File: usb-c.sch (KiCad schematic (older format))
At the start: 55 parts, among them J201 USB_C_Receptacle, U201 PTN5110HQZ, U202 PTN36043BXZ, U203 PCMF3HDMI2SZ, U204 PCMF2HDMI2SZ, U205 TLV3201AIDBVR

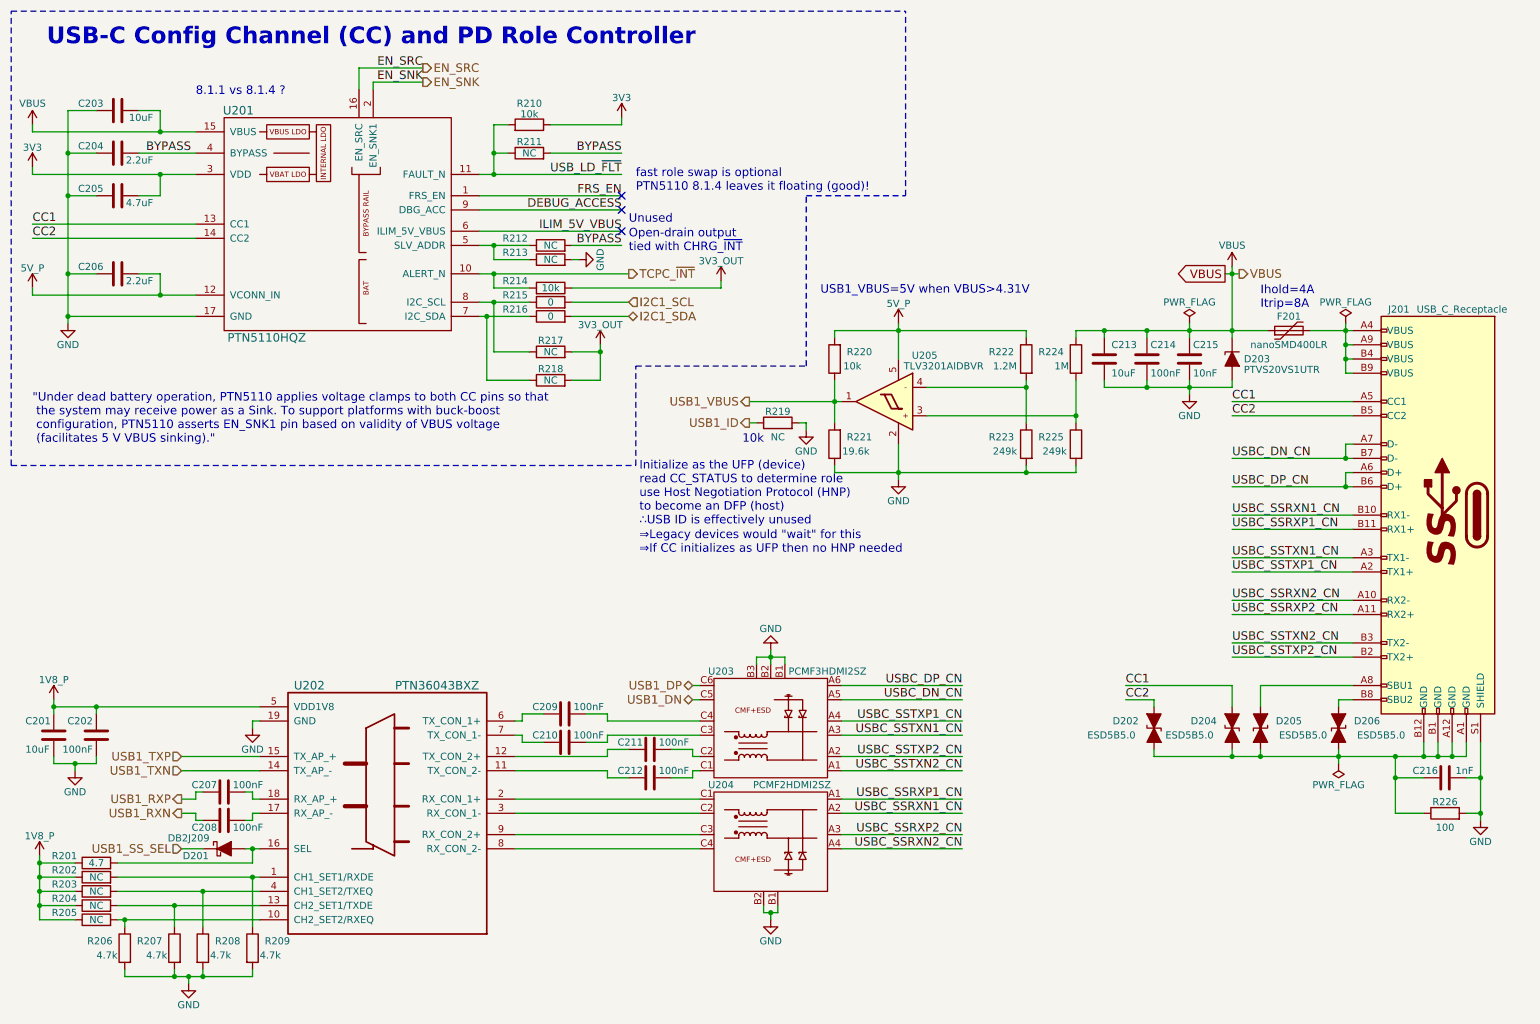
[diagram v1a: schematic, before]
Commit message: Begin GNSS schematic using MAX-M8 module
Since UART2 isn't brought out then will either need to use UART1 (debug) with jumpers or the module's I2C interface.

Resolve merge conflict after pulling recent commit, now can no longer use SSH (since Gogs is getting abandoned?).
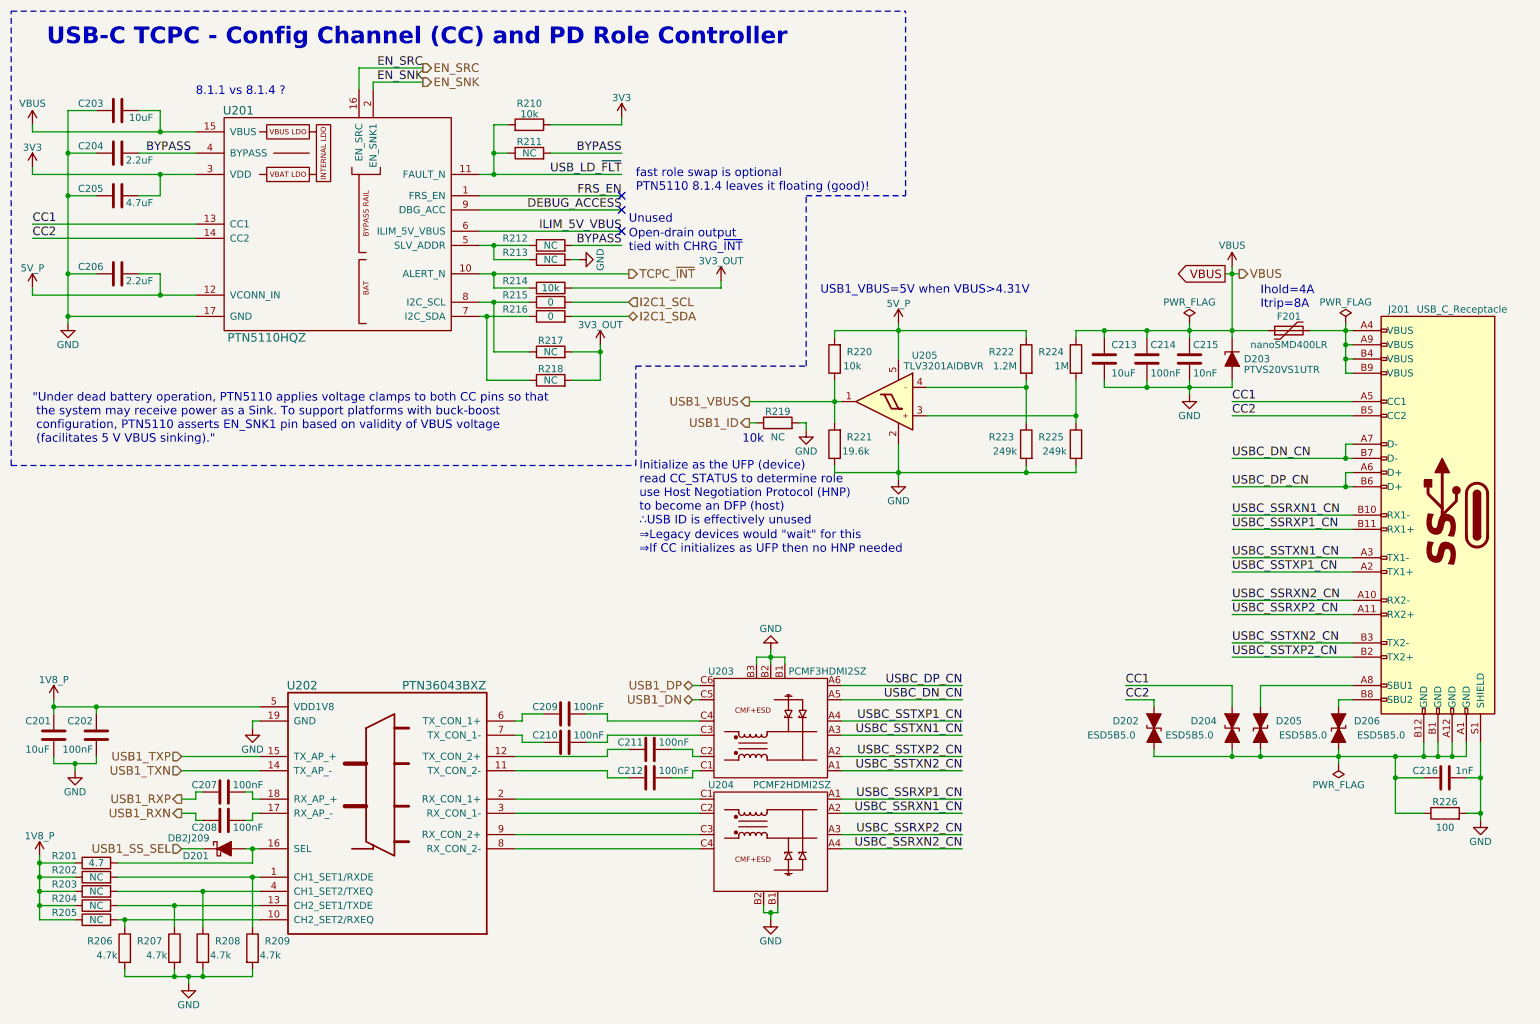
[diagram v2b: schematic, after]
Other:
- note added: "USB-C TCPC - Config Channel (CC) and PD Role Controller"
- note removed: "USB-C Config Channel (CC) and PD Role Controller"
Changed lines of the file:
@@
 $Descr A4 11693 8268
 encoding utf-8
-Sheet 2 23
+Sheet 2 24
 Title "USB Type C"
 Date "2018-05-23"
@@
 Ihold=4A\nItrip=8A
 Text Notes 750  750  0    118  ~ 24
-USB-C Config Channel (CC) and PD Role Controller
+USB-C TCPC - Config Channel (CC) and PD Role Controller
 $Comp
 L USB_C_Receptacle J201
@@
 U 1 1 5AECBE93
 P 3150 6200
-F 0 "U202" H 2600 7150 60  0000 C CNN
-F 1 "PTN36043BXZ" H 3500 7150 60  0000 C CNN
+F 0 "U202" H 2550 7150 60  0000 C CNN
+F 1 "PTN36043BXZ" H 3550 7150 60  0000 C CNN
 F 2 "" H 3150 6350 60  0001 C CNN
 F 3 "https://www.nxp.com/docs/en/data-sheet/PTN36043.pdf" H 3150 6350 60  0001 C CNN

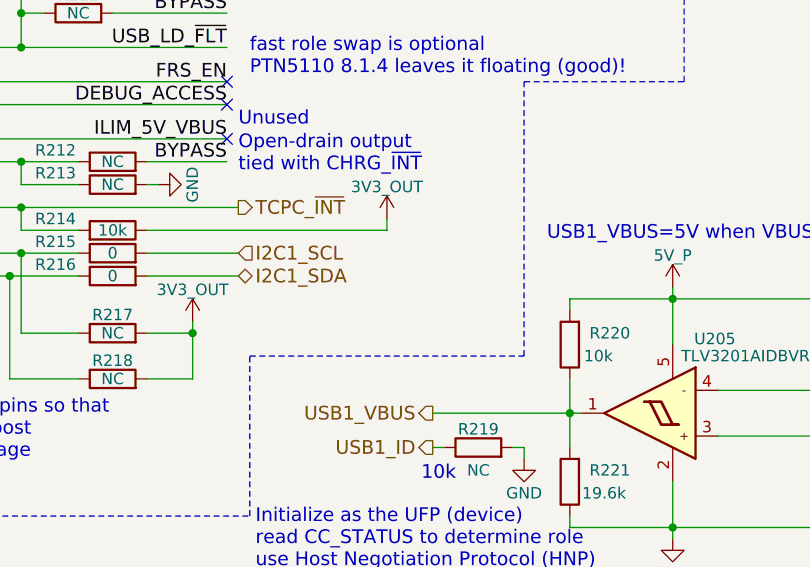
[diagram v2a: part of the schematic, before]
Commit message: Include address in schematic notes for all I2C1 slaves, make HDMI connector shielding resistor to GND 0Ohms
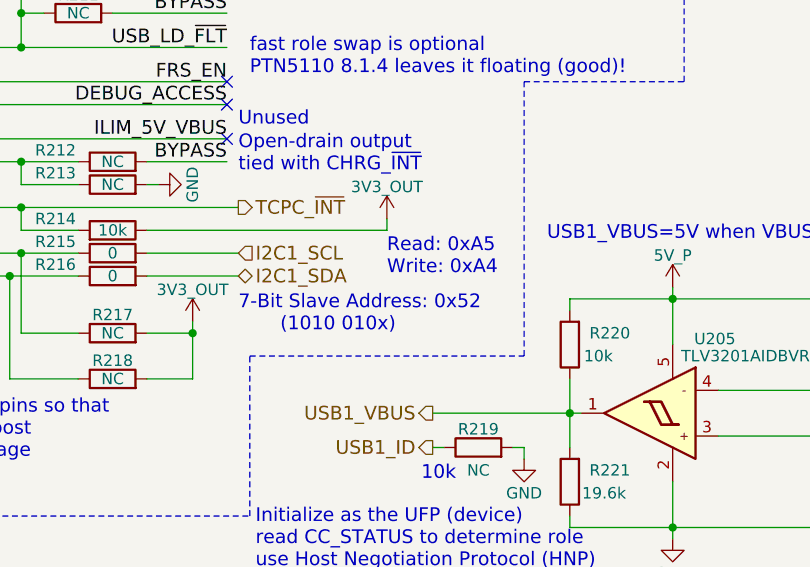
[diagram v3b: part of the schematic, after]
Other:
- note added: "7-Bit Slave Address: 0x52\n (1010 010x)"
- note added: "Read: 0xA5\nWrite: 0xA4"
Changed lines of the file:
@@
 	1    0    0    -1
 $EndComp
+Text Notes 4850 2900 0    60   ~ 0
+7-Bit Slave Address: 0x52\n       (1010 010x)
+Text Notes 5500 2650 0    60   ~ 0
+Read: 0xA5\nWrite: 0xA4
 $EndSCHEMATC

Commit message: Assign most of the capacitors their respective footprints (most are 0603s), add camera/CSI connector component info, source cheaper distributors for 3.5mm headset jack and RJ45
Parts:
- C202, C204, C205, C206, C207, C208, C209, C210, C211, C212, C214, C215, C216: footprint (none) -> Capacitors_SMD:C_0603
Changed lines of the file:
@@
 F 0 "C204" V 1300 1600 50  0000 L CNN
 F 1 "2.2uF" V 1200 1250 50  0000 L CNN
-F 2 "" H 1288 1350 50  0001 C CNN
+F 2 "Capacitors_SMD:C_0603" H 1288 1350 50  0001 C CNN
 F 3 "" H 1250 1500 50  0001 C CNN
 	1    1250 1500
@@
 F 0 "C205" V 1300 1900 50  0000 L CNN
 F 1 "4.7uF" V 1200 1550 50  0000 L CNN
-F 2 "" H 1288 1650 50  0001 C CNN
+F 2 "Capacitors_SMD:C_0603" H 1288 1650 50  0001 C CNN
 F 3 "" H 1250 1800 50  0001 C CNN
 	1    1250 1800
@@
 F 0 "C206" V 1300 2450 50  0000 L CNN
 F 1 "2.2uF" V 1200 2100 50  0000 L CNN
-F 2 "" H 1288 2200 50  0001 C CNN
+F 2 "Capacitors_SMD:C_0603" H 1288 2200 50  0001 C CNN
 F 3 "" H 1250 2350 50  0001 C CNN
 	1    1250 2350
@@
 $EndComp
 $Comp
-L GND #PWR210
+L GND #PWR030
 U 1 1 5ADED127
 P 4500 2250
-F 0 "#PWR210" H 4500 2000 50  0001 C CNN
+F 0 "#PWR030" H 4500 2000 50  0001 C CNN
 F 1 "GND" H 4500 2100 50  0000 C CNN
 F 2 "" H 4500 2250 50  0001 C CNN
@@
 $EndComp
 $Comp
-L 3V3_OUT #PWR211
+L 3V3_OUT #PWR031
 U 1 1 5ADED151
 P 4650 2850
-F 0 "#PWR211" H 4650 2700 50  0001 C CNN
+F 0 "#PWR031" H 4650 2700 50  0001 C CNN
 F 1 "3V3_OUT" H 4650 2990 50  0000 C CNN
 F 2 "" H 4650 2850 50  0001 C CNN
@@
 $EndComp
 $Comp
-L 3V3_OUT #PWR213
+L 3V3_OUT #PWR032
 U 1 1 5ADED157
 P 5500 2400
-F 0 "#PWR213" H 5500 2250 50  0001 C CNN
+F 0 "#PWR032" H 5500 2250 50  0001 C CNN
 F 1 "3V3_OUT" H 5500 2540 50  0000 C CNN
 F 2 "" H 5500 2400 50  0001 C CNN
@@
 $EndComp
 $Comp
-L GND #PWR206
+L GND #PWR033
 U 1 1 5ADED15E
 P 900 2700
-F 0 "#PWR206" H 900 2450 50  0001 C CNN
+F 0 "#PWR033" H 900 2450 50  0001 C CNN
 F 1 "GND" H 900 2550 50  0000 C CNN
 F 2 "" H 900 2700 50  0001 C CNN
@@
 $EndComp
 $Comp
-L GND #PWR209
+L GND #PWR034
 U 1 1 5AECC278
 P 2200 5550
-F 0 "#PWR209" H 2200 5300 50  0001 C CNN
+F 0 "#PWR034" H 2200 5300 50  0001 C CNN
 F 1 "GND" H 2200 5400 50  0000 C CNN
 F 2 "" H 2200 5550 50  0001 C CNN
@@
 F 0 "C207" V 2050 6050 50  0000 L CNN
 F 1 "100nF" V 2050 5725 50  0000 L CNN
-F 2 "" H 2038 5850 50  0001 C CNN
+F 2 "Capacitors_SMD:C_0603" H 2038 5850 50  0001 C CNN
 F 3 "" H 2000 6000 50  0001 C CNN
 	1    2000 6000
@@
 F 0 "C208" V 2050 6250 50  0000 L CNN
 F 1 "100nF" V 2050 5925 50  0000 L CNN
-F 2 "" H 2038 6050 50  0001 C CNN
+F 2 "Capacitors_SMD:C_0603" H 2038 6050 50  0001 C CNN
 F 3 "" H 2000 6200 50  0001 C CNN
 	1    2000 6200
@@
 F 0 "C202" H 1125 5700 50  0000 L CNN
 F 1 "100nF" H 1125 5500 50  0000 L CNN
-F 2 "" H 1138 5450 50  0001 C CNN
+F 2 "Capacitors_SMD:C_0603" H 1138 5450 50  0001 C CNN
 F 3 "" H 1100 5600 50  0001 C CNN
 	1    1100 5600
@@
 $EndComp
 $Comp
-L GND #PWR207
+L GND #PWR035
 U 1 1 5AED260D
 P 950 5850
-F 0 "#PWR207" H 950 5600 50  0001 C CNN
+F 0 "#PWR035" H 950 5600 50  0001 C CNN
 F 1 "GND" H 950 5700 50  0000 C CNN
 F 2 "" H 950 5850 50  0001 C CNN
@@
 $EndComp
 $Comp
-L GND #PWR208
+L GND #PWR036
 U 1 1 5AED9A25
 P 1750 7350
-F 0 "#PWR208" H 1750 7100 50  0001 C CNN
+F 0 "#PWR036" H 1750 7100 50  0001 C CNN
 F 1 "GND" H 1750 7200 50  0000 C CNN
 F 2 "" H 1750 7350 50  0001 C CNN
@@
 $EndComp
 $Comp
-L 1V8_P #PWR204
+L 1V8_P #PWR037
 U 1 1 5AEE2251
 P 700 6450
-F 0 "#PWR204" H 700 6300 50  0001 C CNN
+F 0 "#PWR037" H 700 6300 50  0001 C CNN
 F 1 "1V8_P" H 700 6590 50  0000 C CNN
 F 2 "" H 700 6450 50  0001 C CNN
@@
 F 0 "C209" V 4450 5500 50  0000 L CNN
 F 1 "100nF" V 4450 5175 50  0000 L CNN
-F 2 "" H 4438 5300 50  0001 C CNN
+F 2 "Capacitors_SMD:C_0603" H 4438 5300 50  0001 C CNN
 F 3 "" H 4400 5450 50  0001 C CNN
 	1    4400 5450
@@
 F 0 "C210" V 4450 5700 50  0000 L CNN
 F 1 "100nF" V 4450 5375 50  0000 L CNN
-F 2 "" H 4438 5500 50  0001 C CNN
+F 2 "Capacitors_SMD:C_0603" H 4438 5500 50  0001 C CNN
 F 3 "" H 4400 5650 50  0001 C CNN
 	1    4400 5650
@@
 F 0 "C211" V 5050 5750 50  0000 L CNN
 F 1 "100nF" V 5050 5425 50  0000 L CNN
-F 2 "" H 5038 5550 50  0001 C CNN
+F 2 "Capacitors_SMD:C_0603" H 5038 5550 50  0001 C CNN
 F 3 "" H 5000 5700 50  0001 C CNN
 	1    5000 5700
@@
 F 0 "C212" V 5050 5950 50  0000 L CNN
 F 1 "100nF" V 5050 5625 50  0000 L CNN
-F 2 "" H 5038 5750 50  0001 C CNN
+F 2 "Capacitors_SMD:C_0603" H 5038 5750 50  0001 C CNN
 F 3 "" H 5000 5900 50  0001 C CNN
 	1    5000 5900
@@
 $EndComp
 $Comp
-L GND #PWR219
+L GND #PWR038
 U 1 1 5AF3BA54
 P 8800 3200
-F 0 "#PWR219" H 8800 2950 50  0001 C CNN
+F 0 "#PWR038" H 8800 2950 50  0001 C CNN
 F 1 "GND" H 8800 3050 50  0000 C CNN
 F 2 "" H 8800 3200 50  0001 C CNN
@@
 F 0 "C215" H 8825 3050 50  0000 L CNN
 F 1 "10nF" H 8825 2850 50  0000 L CNN
-F 2 "" H 8838 2800 50  0001 C CNN
+F 2 "Capacitors_SMD:C_0603" H 8838 2800 50  0001 C CNN
 F 3 "" H 8800 2950 50  0001 C CNN
 	1    8800 2950
@@
 F 0 "C214" H 8525 3050 50  0000 L CNN
 F 1 "100nF" H 8525 2850 50  0000 L CNN
-F 2 "" H 8538 2800 50  0001 C CNN
+F 2 "Capacitors_SMD:C_0603" H 8538 2800 50  0001 C CNN
 F 3 "" H 8500 2950 50  0001 C CNN
 	1    8500 2950
@@
 $EndComp
 $Comp
-L GND #PWR218
+L GND #PWR039
 U 1 1 5AF4F7E8
 P 6750 3800
-F 0 "#PWR218" H 6750 3550 50  0001 C CNN
+F 0 "#PWR039" H 6750 3550 50  0001 C CNN
 F 1 "GND" H 6750 3650 50  0000 C CNN
 F 2 "" H 6750 3800 50  0001 C CNN
@@
 $EndComp
 $Comp
-L GND #PWR216
+L GND #PWR040
 U 1 1 5AF595A0
 P 6100 3450
-F 0 "#PWR216" H 6100 3200 50  0001 C CNN
+F 0 "#PWR040" H 6100 3200 50  0001 C CNN
 F 1 "GND" H 6100 3300 50  0000 C CNN
 F 2 "" H 6100 3450 50  0001 C CNN
@@
 $EndComp
 $Comp
-L GND #PWR215
+L GND #PWR041
 U 1 1 5AF8A55A
 P 5850 6900
-F 0 "#PWR215" H 5850 6650 50  0001 C CNN
+F 0 "#PWR041" H 5850 6650 50  0001 C CNN
 F 1 "GND" H 5850 6750 50  0000 C CNN
 F 2 "" H 5850 6900 50  0001 C CNN
@@
 $EndComp
 $Comp
-L GND #PWR214
+L GND #PWR042
 U 1 1 5AF8A8ED
 P 5850 5000
-F 0 "#PWR214" H 5850 4750 50  0001 C CNN
+F 0 "#PWR042" H 5850 4750 50  0001 C CNN
 F 1 "GND" H 5850 4850 50  0000 C CNN
 F 2 "" H 5850 5000 50  0001 C CNN
@@
 F 0 "C216" V 10650 5950 50  0000 L CNN
 F 1 "1nF" V 10650 5700 50  0000 L CNN
-F 2 "" H 10638 5750 50  0001 C CNN
+F 2 "Capacitors_SMD:C_0603" H 10638 5750 50  0001 C CNN
 F 3 "" H 10600 5900 50  0001 C CNN
 	1    10600 5900
@@
 	10850 6150 10750 6150
 $Comp
-L GND #PWR221
+L GND #PWR043
 U 1 1 5AFA9EDB
 P 10850 6200
-F 0 "#PWR221" H 10850 5950 50  0001 C CNN
+F 0 "#PWR043" H 10850 5950 50  0001 C CNN
 F 1 "GND" H 10850 6050 50  0000 C CNN
 F 2 "" H 10850 6200 50  0001 C CNN
@@
 	500  3700 500  500
 $Comp
-L 1V8_P #PWR205
+L 1V8_P #PWR044
 U 1 1 5B02622C
 P 800 5350
-F 0 "#PWR205" H 800 5200 50  0001 C CNN
+F 0 "#PWR044" H 800 5200 50  0001 C CNN
 F 1 "1V8_P" H 800 5490 50  0000 C CNN
 F 2 "" H 800 5350 50  0001 C CNN
@@
 Connection ~ 800  5400
 $Comp
-L PWR_FLAG #FLG202
+L PWR_FLAG #FLG045
 U 1 1 5B0A460D
 P 9850 5800
-F 0 "#FLG202" H 9850 5875 50  0001 C CNN
+F 0 "#FLG045" H 9850 5875 50  0001 C CNN
 F 1 "PWR_FLAG" H 9850 5950 50  0000 C CNN
 F 2 "" H 9850 5800 50  0001 C CNN
@@
 USB1_VBUS=5V when VBUS>4.31V
 $Comp
-L VBUS #PWR220
+L VBUS #PWR046
 U 1 1 5AF2D1E1
 P 9100 2300
-F 0 "#PWR220" H 9100 2150 50  0001 C CNN
+F 0 "#PWR046" H 9100 2150 50  0001 C CNN
 F 1 "VBUS" H 9100 2450 50  0000 C CNN
 F 2 "" H 9100 2300 50  0001 C CNN
@@
 $EndComp
 $Comp
-L PWR_FLAG #FLG201
+L PWR_FLAG #FLG047
 U 1 1 5AF2D52F
 P 8800 2700
-F 0 "#FLG201" H 8800 2775 50  0001 C CNN
+F 0 "#FLG047" H 8800 2775 50  0001 C CNN
 F 1 "PWR_FLAG" H 8800 2850 50  0000 C CNN
 F 2 "" H 8800 2700 50  0001 C CNN
@@
 NoConn ~ 4800 2050
 $Comp
-L VBUS #PWR201
+L VBUS #PWR048
 U 1 1 5AF6C71F
 P 650 1300
-F 0 "#PWR201" H 650 1150 50  0001 C CNN
+F 0 "#PWR048" H 650 1150 50  0001 C CNN
 F 1 "VBUS" H 650 1450 50  0000 C CNN
 F 2 "" H 650 1300 50  0001 C CNN
@@
 NoConn ~ 4800 1800
 $Comp
-L PWR_FLAG #FLG203
+L PWR_FLAG #FLG049
 U 1 1 5AF77F57
 P 9900 2700
-F 0 "#FLG203" H 9900 2775 50  0001 C CNN
+F 0 "#FLG049" H 9900 2775 50  0001 C CNN
 F 1 "PWR_FLAG" H 9900 2850 50  0000 C CNN
 F 2 "" H 9900 2700 50  0001 C CNN
@@
 	9050 2350 9150 2350
 $Comp
-L 3V3 #PWR212
+L 3V3 #PWR050
 U 1 1 5B39F466
 P 4800 1250
-F 0 "#PWR212" H 4800 1100 50  0001 C CNN
+F 0 "#PWR050" H 4800 1100 50  0001 C CNN
 F 1 "3V3" H 4800 1390 50  0000 C CNN
 F 2 "" H 4800 1250 50  0001 C CNN
@@
 $EndComp
 $Comp
-L 3V3 #PWR202
+L 3V3 #PWR051
 U 1 1 5B39F890
 P 650 1600
-F 0 "#PWR202" H 650 1450 50  0001 C CNN
+F 0 "#PWR051" H 650 1450 50  0001 C CNN
 F 1 "3V3" H 650 1740 50  0000 C CNN
 F 2 "" H 650 1600 50  0001 C CNN
@@
 $EndComp
 $Comp
-L 5V_P #PWR203
+L 5V_P #PWR052
 U 1 1 5B3E3D9A
 P 650 2450
-F 0 "#PWR203" H 650 2300 50  0001 C CNN
+F 0 "#PWR052" H 650 2300 50  0001 C CNN
 F 1 "5V_P" H 650 2590 50  0000 C CNN
 F 2 "" H 650 2450 50  0001 C CNN
@@
 $EndComp
 $Comp
-L 5V_P #PWR217
+L 5V_P #PWR053
 U 1 1 5B3E4B11
 P 6750 2700
-F 0 "#PWR217" H 6750 2550 50  0001 C CNN
+F 0 "#PWR053" H 6750 2550 50  0001 C CNN
 F 1 "5V_P" H 6750 2840 50  0000 C CNN
 F 2 "" H 6750 2700 50  0001 C CNN

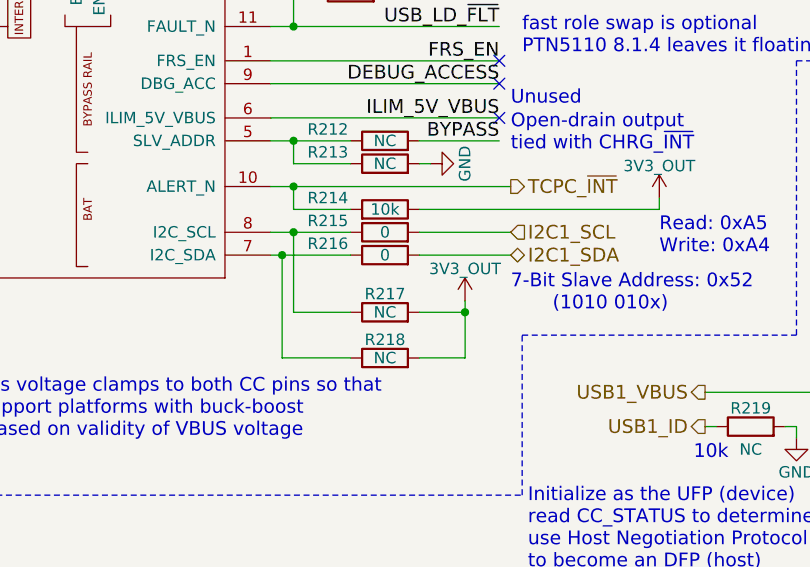
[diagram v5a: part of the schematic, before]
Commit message: Make corrections to schematic based on Emcraft's baseboard revision changes
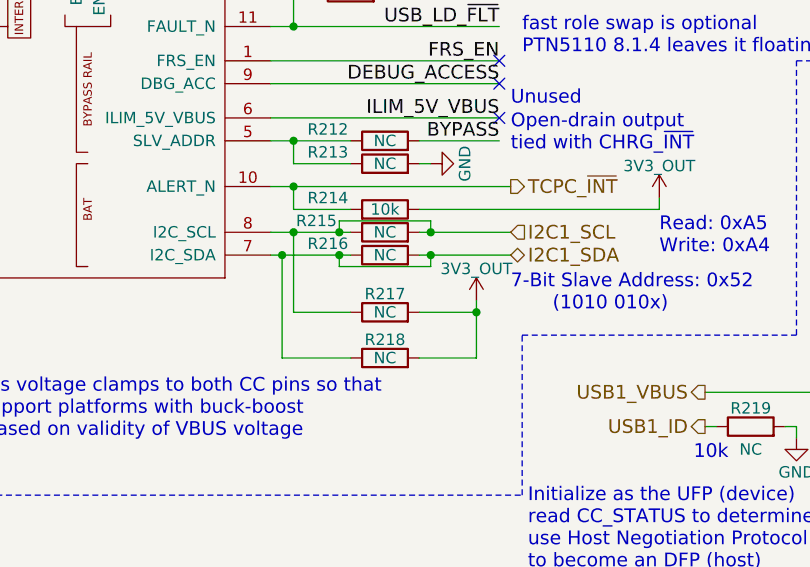
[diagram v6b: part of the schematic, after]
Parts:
- R215, R216: value 0 -> NC
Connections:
- net I2C1_SCL: now also R215.1, R217.1, U201.8 (I2C_SCL)
- net I2C1_SDA: now also R216.1, R218.1, U201.7 (I2C_SDA)
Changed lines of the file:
@@
 Sheet 2 24
 Title "USB Type C"
-Date "2018-05-31"
+Date "2018-06-01"
 Rev "v0.1.0"
 Comp "Purism SPC"
@@
 U 1 1 5ADED135
 P 4300 2550
-F 0 "R215" V 4350 2800 50  0000 C CNN
-F 1 "0" V 4300 2550 50  0000 C CNN
+F 0 "R215" V 4350 2850 50  0000 C CNN
+F 1 "NC" V 4300 2550 50  0000 C CNN
 F 2 "Resistors_SMD:R_0603" V 4230 2550 50  0001 C CNN
 F 3 "" H 4300 2550 50  0001 C CNN
@@
 P 4300 2650
 F 0 "R216" V 4350 2900 50  0000 C CNN
-F 1 "0" V 4300 2650 50  0000 C CNN
+F 1 "NC" V 4300 2650 50  0000 C CNN
 F 2 "Resistors_SMD:R_0603" V 4230 2650 50  0001 C CNN
 F 3 "" H 4300 2650 50  0001 C CNN
@@
 L 3V3_OUT #PWR031
 U 1 1 5ADED151
-P 4650 2850
-F 0 "#PWR031" H 4650 2700 50  0001 C CNN
-F 1 "3V3_OUT" H 4650 2990 50  0000 C CNN
-F 2 "" H 4650 2850 50  0001 C CNN
-F 3 "" H 4650 2850 50  0001 C CNN
-	1    4650 2850
+P 4700 2850
+F 0 "#PWR031" H 4700 2700 50  0001 C CNN
+F 1 "3V3_OUT" H 4700 2990 50  0000 C CNN
+F 2 "" H 4700 2850 50  0001 C CNN
+F 3 "" H 4700 2850 50  0001 C CNN
+	1    4700 2850
 	1    0    0    -1
 $EndComp
@@
 Connection ~ 3850 2650
 Wire Wire Line
-	4450 2900 4650 2900
-Wire Wire Line
-	4650 2850 4650 3100
-Wire Wire Line
-	4650 3100 4450 3100
-Connection ~ 4650 2900
+	4450 2900 4700 2900
+Wire Wire Line
+	4700 2850 4700 3100
+Wire Wire Line
+	4700 3100 4450 3100
+Connection ~ 4700 2900
 Wire Wire Line
 	4450 2450 5500 2450
@@
 Text Notes 5500 2650 0    60   ~ 0
 Read: 0xA5\nWrite: 0xA4
+Wire Wire Line
+	4500 2650 4500 2700
+Wire Wire Line
+	4500 2700 4100 2700
+Wire Wire Line
+	4100 2700 4100 2650
+Connection ~ 4100 2650
+Connection ~ 4500 2650
+Wire Wire Line
+	4100 2550 4100 2500
+Wire Wire Line
+	4100 2500 4500 2500
+Wire Wire Line
+	4500 2500 4500 2550
+Connection ~ 4500 2550
+Connection ~ 4100 2550
 $EndSCHEMATC
